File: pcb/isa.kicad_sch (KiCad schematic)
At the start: 30 parts, among them J1 Bus_ISA_16bit, J10 ISA_DEBUG, J15 PC SPK, J17 IOout, J2 Bus_ISA_16bit, U10 8259A-2, U23 74LS573, U9 8254, Y1 TXC-7C

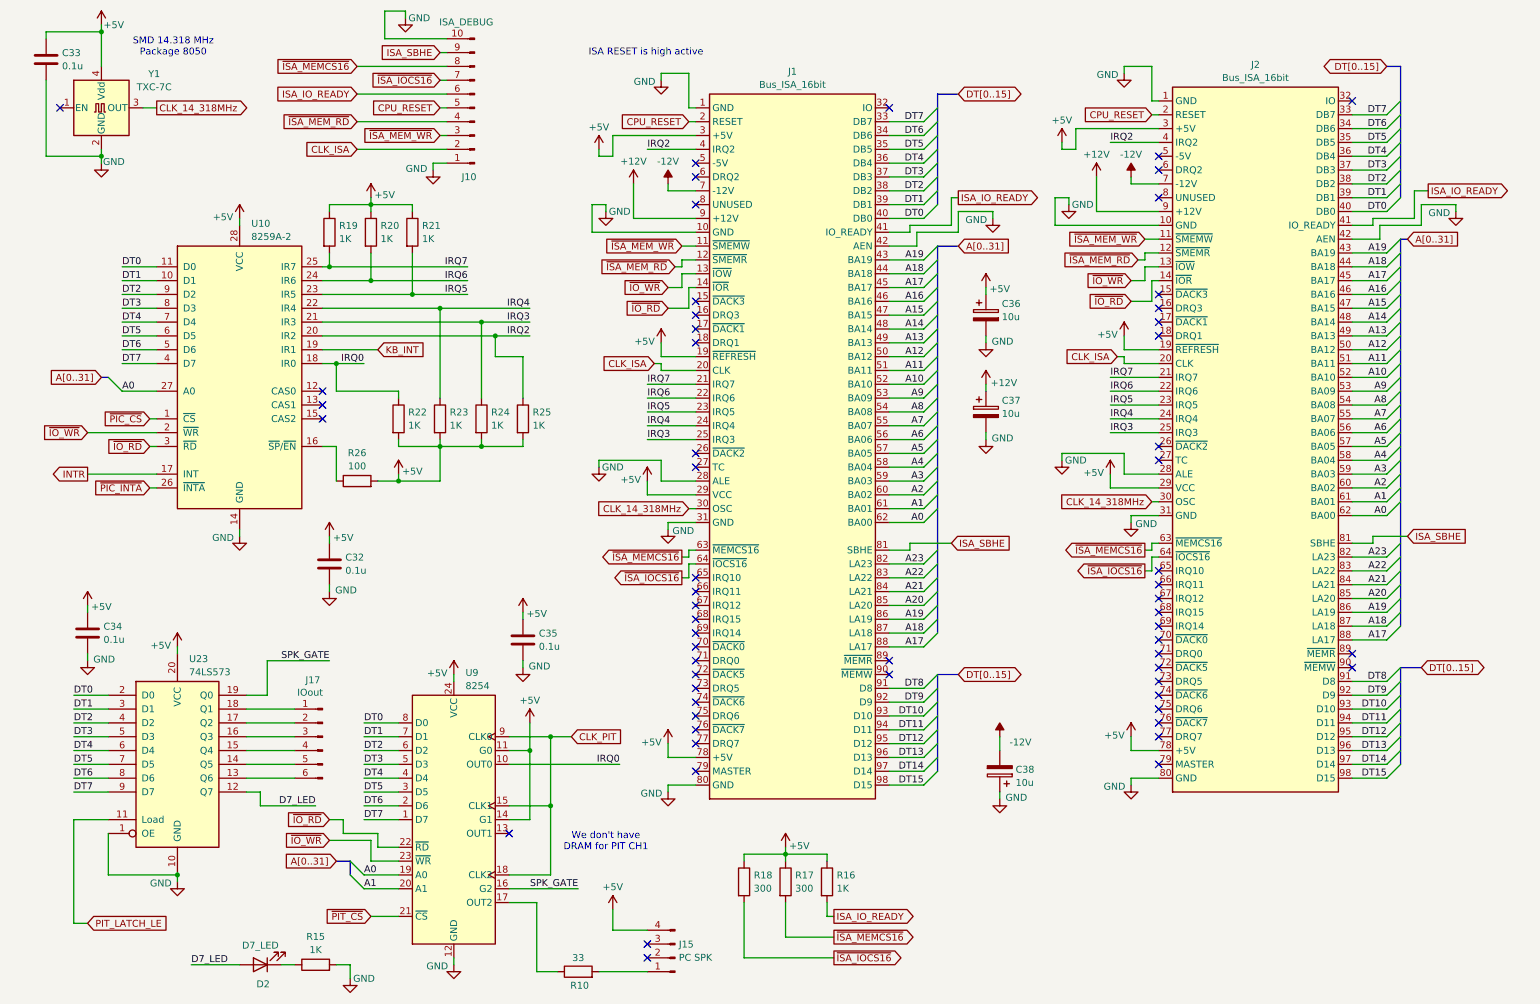
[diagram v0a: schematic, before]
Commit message: Add fpga sources, update schematic, update README
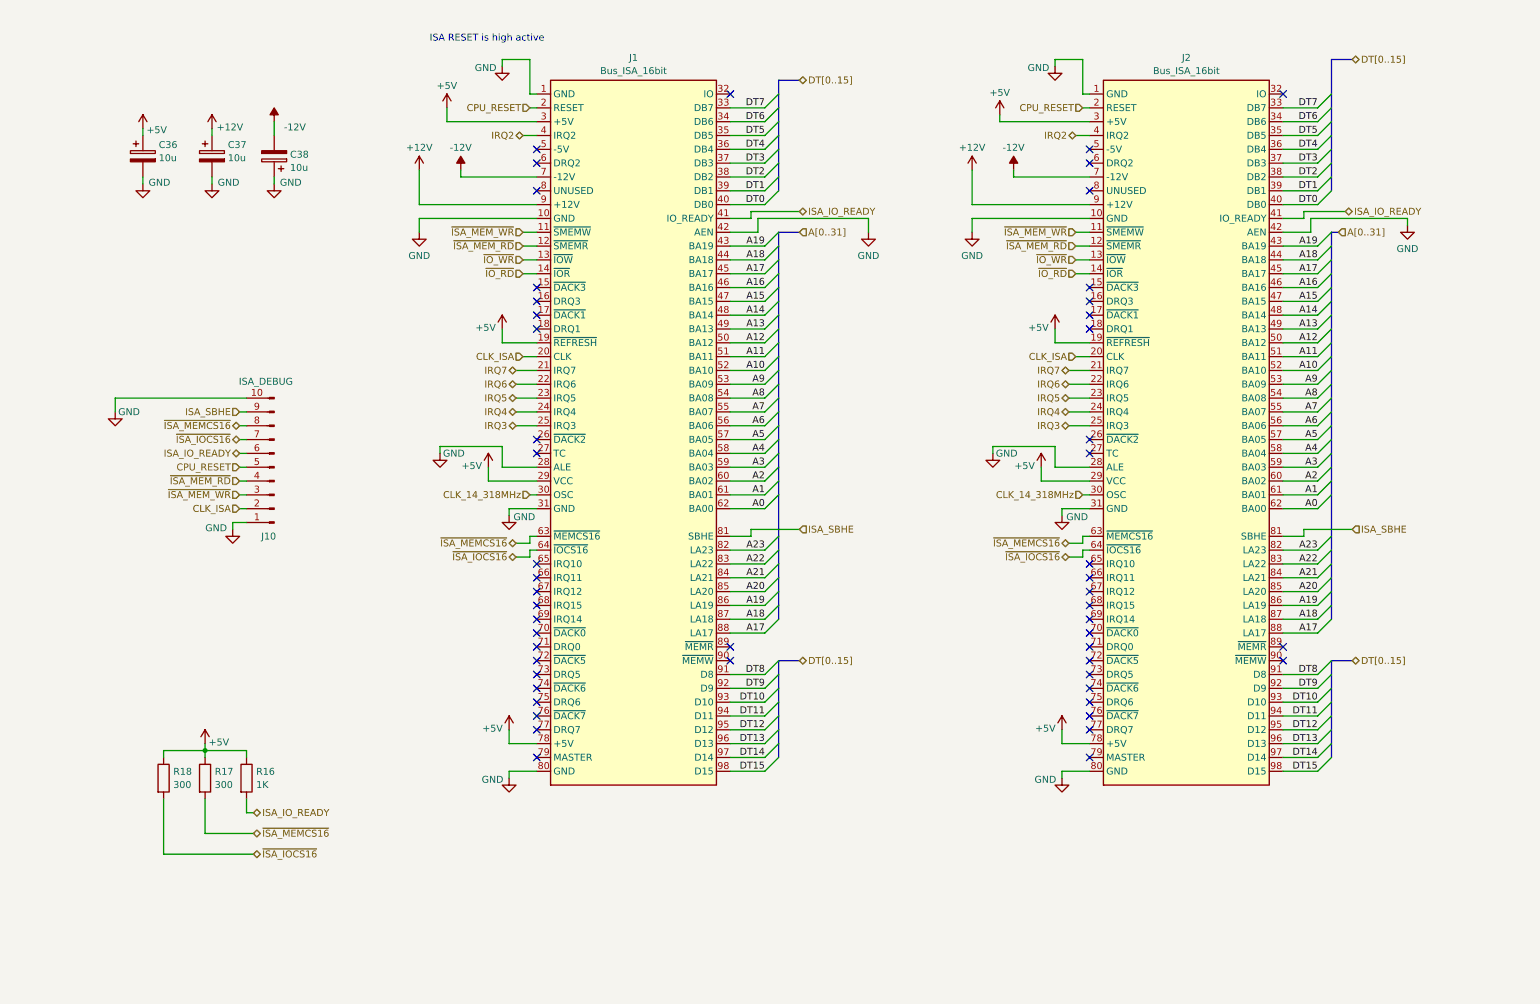
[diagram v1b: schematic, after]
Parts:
- removed C32, C33, C34, C35: 0.1u, Capacitor_SMD:C_0805_2012Metric_Pad1.18x1.45mm_HandSolder, symbol Device:C
- removed D2: D7_LED, LED_THT:LED_D4.0mm, symbol Device:LED
- removed J15: PC SPK, Connector_PinHeader_2.54mm:PinHeader_1x04_P2.54mm_Vertical, symbol Connector:Conn_01x04_Pin
- removed J17: IOout, Connector_PinHeader_2.54mm:PinHeader_1x06_P2.54mm_Vertical, symbol Connector:Conn_01x06_Pin
- removed R10: 33, Resistor_SMD:R_0805_2012Metric_Pad1.20x1.40mm_HandSolder, symbol Device:R
- removed R15, R19, R20, R21, R22, R23, R24, R25: 1K, Resistor_SMD:R_0805_2012Metric_Pad1.20x1.40mm_HandSolder, symbol Device:R
- removed R26: 100, Resistor_SMD:R_0805_2012Metric_Pad1.20x1.40mm_HandSolder, symbol Device:R
- removed U10: 8259A-2, Package_LCC:PLCC-28_THT-Socket, symbol Interface:8259A-2
- removed U23: 74LS573, Package_SO:SOP-20_7.5x12.8mm_P1.27mm, symbol 74xx:74LS573
- removed U9: 8254, Package_DIP:DIP-24_W15.24mm, symbol Timer:8254
- removed Y1: TXC-7C, Oscillator:Oscillator_SMD_SeikoEpson_SG8002CA-4Pin_7.0x5.0mm_HandSoldering, symbol Oscillator:TXC-7C
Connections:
- no-connect marks 59 -> 52
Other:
- note removed: "SMD 14.318 MHz Package 8050"
- note removed: "We don't have DRAM for PIT CH1"
- moved on the sheet: C36, C37, C38, J1, J10, J2, R16, R17, R18

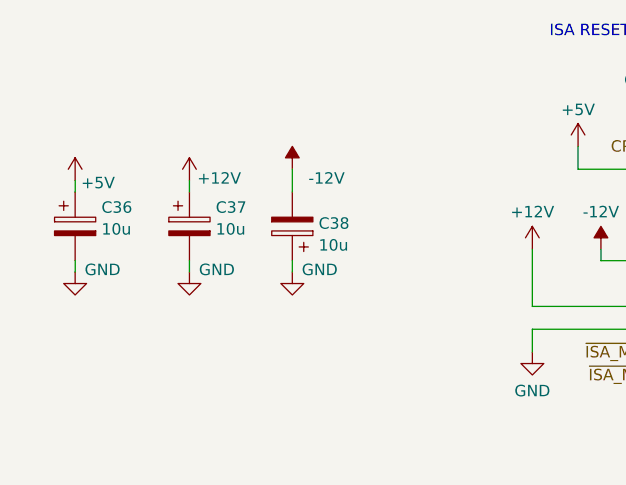
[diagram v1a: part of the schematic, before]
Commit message: C36 use same 22uF cap for +5V rail, less part variance
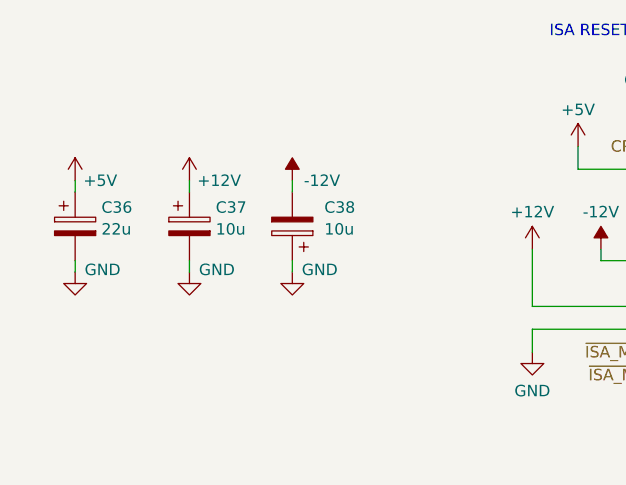
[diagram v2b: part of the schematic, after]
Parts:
- C36: value 10u -> 22u
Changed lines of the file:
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@@
 	(wire
 		(pts
-			(xy 57.15 34.29) (xy 57.15 36.83)
+			(xy 57.15 35.56) (xy 57.15 36.83)
 		)
 		(stroke
@@
 		)
 		(property "Value" "+12V"
-			(at 49.022 35.306 0)
+			(at 49.022 35.56 0)
 			(effects
 				(font
@@
 	(symbol
 		(lib_id "power:-12V")
-		(at 57.15 34.29 0)
+		(at 57.15 35.56 0)
 		(unit 1)
 		(exclude_from_sim no)
@@
 		(dnp no)
 		(property "Reference" "#PWR0139"
-			(at 57.15 38.1 0)
+			(at 57.15 39.37 0)
 			(effects
 				(font
@@
 		)
 		(property "Value" "-12V"
-			(at 60.96 35.306 0)
+			(at 60.452 35.56 0)
 			(effects
 				(font
@@
 		)
 		(property "Footprint" ""
-			(at 57.15 34.29 0)
+			(at 57.15 35.56 0)
 			(effects
 				(font
@@
 		)
 		(property "Datasheet" ""
-			(at 57.15 34.29 0)
+			(at 57.15 35.56 0)
 			(effects
 				(font
@@
 		)
 		(property "Description" "Power symbol creates a global label with name \"-12V\""
-			(at 57.15 34.29 0)
+			(at 57.15 35.56 0)
 			(effects
 				(font
@@
 		(on_board yes)
 		(dnp no)
-		(fields_autoplaced yes)
 		(property "Reference" "C36"
 			(at 35.941 38.5388 0)
@@
 			)
 		)
-		(property "Value" "10u"
+		(property "Value" "22u"
 			(at 35.941 40.9631 0)
 			(effects
@@
 		)
 		(property "Value" "+5V"
-			(at 35.56 35.814 0)
+			(at 35.814 35.56 0)
 			(effects
 				(font
@@
 		(on_board yes)
 		(dnp no)
-		(fields_autoplaced yes)
 		(property "Reference" "C38"
-			(at 60.071 40.3168 0)
+			(at 60.706 38.5388 0)
 			(effects
 				(font
@@
 		)
 		(property "Value" "10u"
-			(at 60.071 42.7411 0)
+			(at 60.706 40.9631 0)
 			(effects
 				(font
